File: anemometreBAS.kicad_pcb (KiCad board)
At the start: 2 copper layers, 1 part

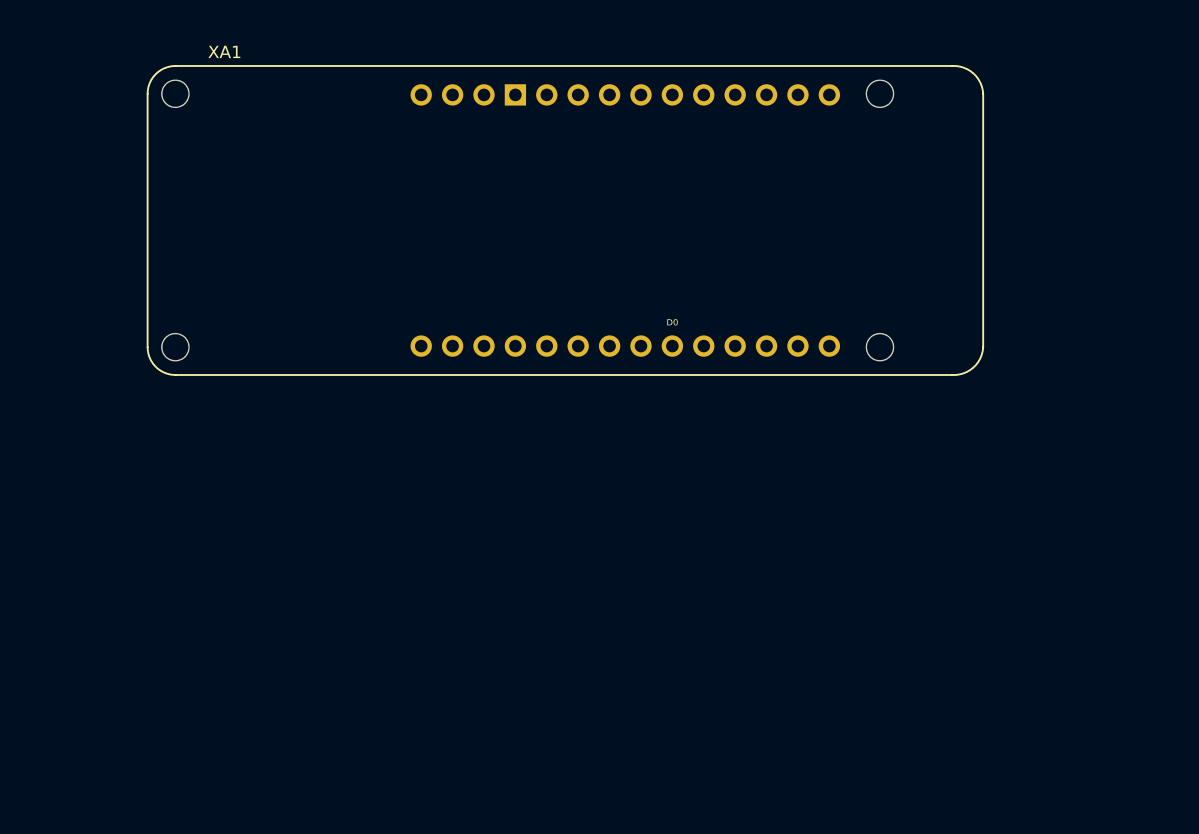
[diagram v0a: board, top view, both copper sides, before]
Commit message: Pcb traversant (#1)
* first pcb version with schematic footprint update

* schematic
	GND at the same pin for each connector
	add M3 hole*3 connected to GND
PCB
	first routing

* Adding 3D model

* route temp sensor data
change +5V net location
change hole location
drc ok only one error with hole under mkr processing board

* pcb without smd resistor
first routing version

* change layer of solar panel and battery mngt card
unshow $Reference and value

* Adding pins socket connectors for MKR1310

* adding optionnal CEM schottky diode
MKR 3D model update

* update 3D models with MKR pin shocket

---------

Co-authored-by: sdaviet <sylvain.daviet@gmail.com>
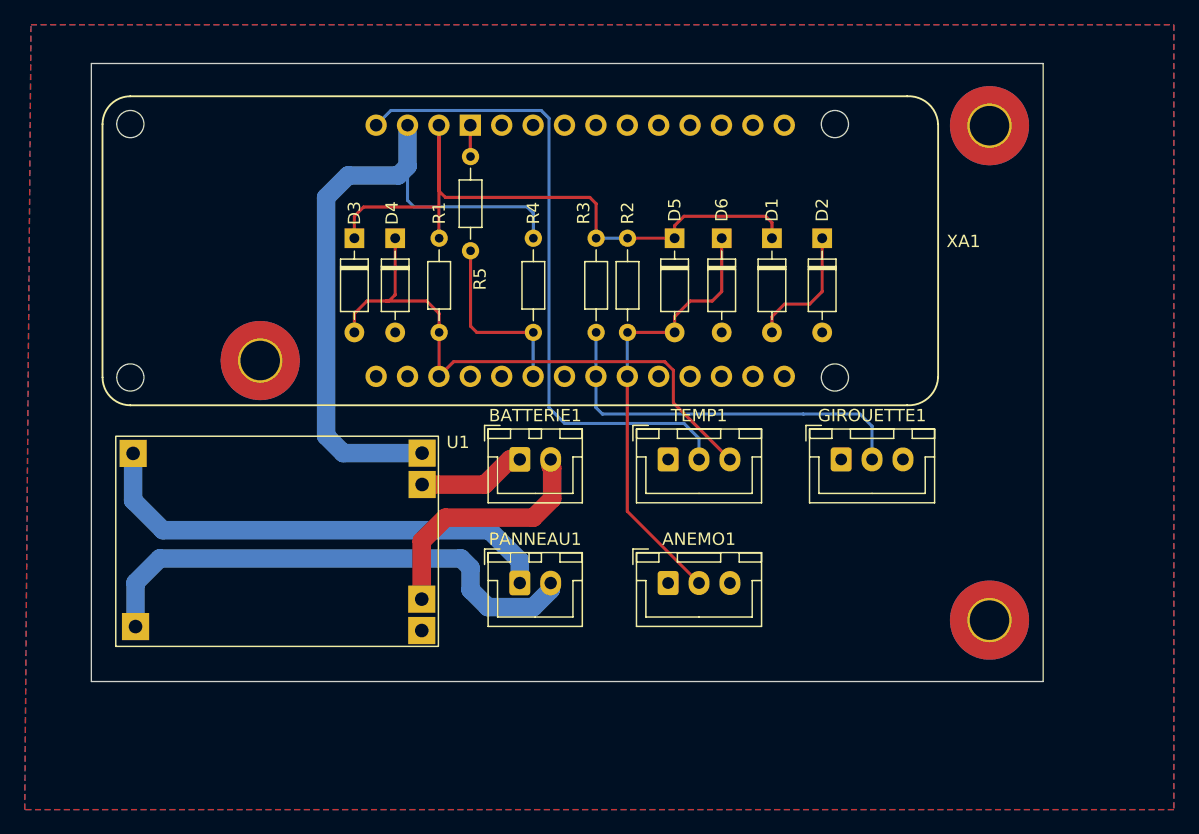
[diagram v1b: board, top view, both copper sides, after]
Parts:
- added ANEMO1: Conn_01x02_Male, Connector_JST:JST_XH_B3B-XH-A_1x03_P2.50mm_Vertical, F.Cu at (144.0, 98.0)
- added BATTERIE1: Conn_01x02_Male, Connector_JST:JST_XH_B2B-XH-A_1x02_P2.50mm_Vertical, F.Cu at (132.0, 88.0)
- added D1: D_Schottky, Diode_THT:D_DO-35_SOD27_P7.62mm_Horizontal, F.Cu at (152.4, 70.1)
- added D2: D_Schottky, Diode_THT:D_DO-35_SOD27_P7.62mm_Horizontal, F.Cu at (156.5, 70.1)
- added D3: D_Schottky, Diode_THT:D_DO-35_SOD27_P7.62mm_Horizontal, F.Cu at (118.6, 70.1)
- added D4: D_Schottky, Diode_THT:D_DO-35_SOD27_P7.62mm_Horizontal, F.Cu at (121.9, 70.1)
- added D5: D_Schottky, Diode_THT:D_DO-35_SOD27_P7.62mm_Horizontal, F.Cu at (144.5, 70.1)
- added D6: D_Schottky, Diode_THT:D_DO-35_SOD27_P7.62mm_Horizontal, F.Cu at (148.3, 70.1)
- added GIROUETTE1: Conn_01x02_Male, Connector_JST:JST_XH_B3B-XH-A_1x03_P2.50mm_Vertical, F.Cu at (158.0, 88.0)
- added H2: MountingHole_Pad, MountingHole:MountingHole_3.2mm_M3_Pad_TopBottom, F.Cu at (170.0, 101.0)
- added H3: MountingHole_Pad, MountingHole:MountingHole_3.2mm_M3_Pad_TopBottom, F.Cu at (170.0, 61.0)
- added H4: MountingHole_Pad, MountingHole:MountingHole_3.2mm_M3_Pad_TopBottom, F.Cu at (111.0, 80.0)
- added PANNEAU1: Conn_01x02_Male, Connector_JST:JST_XH_B2B-XH-A_1x02_P2.50mm_Vertical, F.Cu at (132.0, 98.0)
- added R1: 4.7K, Resistor_THT:R_Axial_DIN0204_L3.6mm_D1.6mm_P7.62mm_Horizontal, F.Cu at (125.5, 70.1)
- added R2: 10K, Resistor_THT:R_Axial_DIN0204_L3.6mm_D1.6mm_P7.62mm_Horizontal, F.Cu at (140.7, 77.7)
- added R3: 10K, Resistor_THT:R_Axial_DIN0204_L3.6mm_D1.6mm_P7.62mm_Horizontal, F.Cu at (138.2, 70.1)
- added R4: 1.5K, Resistor_THT:R_Axial_DIN0204_L3.6mm_D1.6mm_P7.62mm_Horizontal, F.Cu at (133.1, 70.1)
- added R5: 2.5K, Resistor_THT:R_Axial_DIN0204_L3.6mm_D1.6mm_P7.62mm_Horizontal, F.Cu at (128.0, 71.1)
- added TEMP1: Conn_01x03_Male, Connector_JST:JST_XH_B3B-XH-A_1x03_P2.50mm_Vertical, F.Cu at (144.0, 88.0)
- added U1: TP4056, TP4056:TP4056, F.Cu at (99.3, 103.1)
- moved XA1 4.39 mm to (100.5, 60.9)
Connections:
- XA1 pad 3V3: unconnected-(XA1-Pad3V3) -> 3V3
- XA1 pad 5V: unconnected-(XA1-Pad5V) -> 5V
- XA1 pad A1: unconnected-(XA1-PadA1) -> Net-(R1-Pad2)
- XA1 pad A4: unconnected-(XA1-PadA4) -> VBridgeBat
- XA1 pad A6: unconnected-(XA1-PadA6) -> VBridgeDir
- XA1 pad D0: unconnected-(XA1-PadD0) -> Net-(XA1-PadD0)
- XA1 pad GND: unconnected-(XA1-PadGND) -> GND
- XA1 pad VIN: unconnected-(XA1-PadVIN) -> VIN
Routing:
- net VIN: track 0.00 -> 57.3 mm
- net 3V3: track 0.00 -> 56.4 mm
- net 5V: track 0.00 -> 53.0 mm
- net Net-(R1-Pad2): track 0.00 -> 48.7 mm
- net VBridgeDir: track 0.00 -> 42.2 mm
- net Net-(PANNEAU1-Pad2): track 0.00 -> 41.8 mm
- net Net-(PANNEAU1-Pad1): track 0.00 -> 38.9 mm
- net Net-(XA1-PadD0): track 0.00 -> 36.7 mm
- net Net-(BATTERIE1-Pad2): track 0.00 -> 19.9 mm
- net VBridgeBat: track 0.00 -> 14.9 mm
- net Net-(BATTERIE1-Pad1): track 0.00 -> 8.74 mm
- net GND: track 0.00 -> 2.55 mm
- added copper zone on B.Cu, net GND
- added copper zone on F.Cu, net GND
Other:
- board outline added: 77 x 50 mm

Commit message: add power connector as jst routing pcb
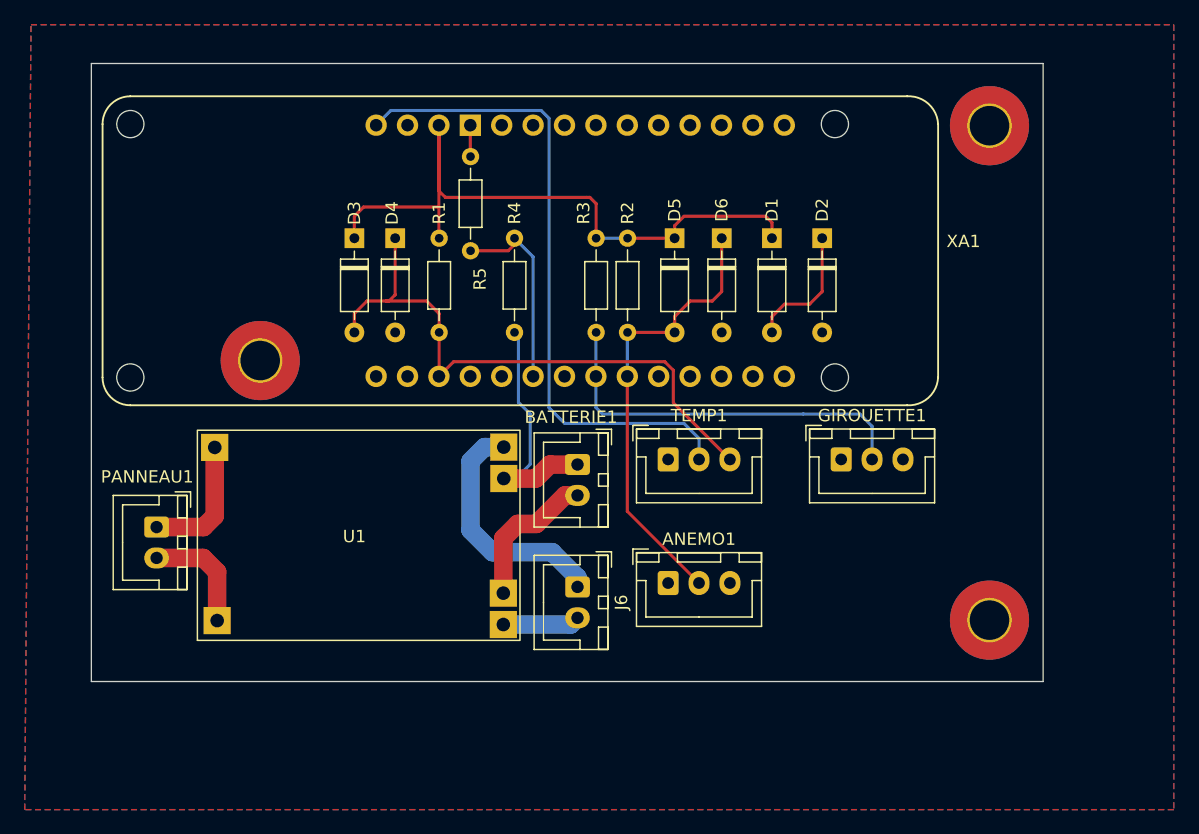
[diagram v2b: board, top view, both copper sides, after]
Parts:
- added J6: Power, Connector_JST:JST_XH_B2B-XH-A_1x02_P2.50mm_Vertical, F.Cu at (136.7, 98.3)
- moved PANNEAU1 29.7 mm to (102.6, 93.5), turned to -90 degrees
- moved R4 7.77 mm to (131.6, 77.7), turned to 90 degrees
- moved U1 6.62 mm to (105.9, 102.6)
- moved BATTERIE1 4.69 mm to (136.7, 88.4), turned to -90 degrees
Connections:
- BATTERIE1 pad 1: Net-(BATTERIE1-Pad1) -> B+
- R4 pad 1: VIN -> B+
- TEMP1 pad 2: 5V -> 3V3
- U1 pad 3: Net-(BATTERIE1-Pad1) -> B+
- U1 pad 5: VIN -> Net-(J6-Pad1)
- XA1 pad VIN: VIN -> unconnected-(XA1-PadVIN)
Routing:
- net VIN: track 57.3 -> 0.00 mm
- net Net-(PANNEAU1-Pad2): track 41.8 -> 9.31 mm
- net Net-(PANNEAU1-Pad1): track 38.9 -> 10.6 mm
- net B+: track 0.00 -> 20.2 mm
- net Net-(J6-Pad1): track 0.00 -> 19.7 mm
- net Net-(BATTERIE1-Pad1): track 8.74 -> 0.00 mm
- net Net-(BATTERIE1-Pad2): track 19.9 -> 11.9 mm
- net GND: track 2.55 -> 8.77 mm
- net VBridgeBat: track 14.9 -> 16.1 mm
